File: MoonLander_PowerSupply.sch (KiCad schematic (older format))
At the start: 17 parts

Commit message: first whack at layout - unrouted
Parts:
- removed C?: 1uF, symbol C
- C201: renamed from C?; value 1Uf -> 1uF; footprint (none) -> Capacitors_SMD:C_0402
- C202, C204: renamed from C?; footprint (none) -> Capacitors_SMD:C_0402
- D201: renamed from D?; footprint (none) -> Diodes_SMD:SOD-323
- D202, D203: renamed from D?; footprint (none) -> LEDs:LED-0603
- IC201: renamed from IC?; footprint (none) -> GrayCatLabs:TI-DSQ
- IC202: renamed from IC?; footprint (none) -> GrayCatLabs:SSOP5
- R201, R202, R203, R204, R205, R206, R207, R208: renamed from R?; footprint (none) -> Resistors_SMD:R_0402
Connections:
- net GND: now also IC201.3 (VSS)
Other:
- moved on the sheet: C202
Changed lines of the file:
@@
 $EndDescr
 $Comp
-L LED D?
+L LED D202
 U 1 1 565F7410
 P 5600 3200
-F 0 "D?" H 5600 3300 50  0000 C CNN
+F 0 "D202" H 5600 3300 50  0000 C CNN
 F 1 "LED" H 5600 3100 50  0000 C CNN
-F 2 "" H 5600 3200 50  0000 C CNN
+F 2 "LEDs:LED-0603" H 5600 3200 50  0001 C CNN
 F 3 "" H 5600 3200 50  0000 C CNN
 	1    5600 3200
@@
 $EndComp
 $Comp
-L R R?
+L R R205
 U 1 1 565F74DB
 P 5350 3600
-F 0 "R?" V 5430 3600 50  0000 C CNN
+F 0 "R205" V 5430 3600 50  0000 C CNN
 F 1 "1k" V 5350 3600 50  0000 C CNN
-F 2 "" V 5280 3600 50  0000 C CNN
+F 2 "Resistors_SMD:R_0402" V 5280 3600 50  0001 C CNN
 F 3 "" H 5350 3600 50  0000 C CNN
 	1    5350 3600
@@
 $EndComp
 $Comp
-L C C?
+L C C201
 U 1 1 565F75E8
 P 2300 3600
-F 0 "C?" H 2325 3700 50  0000 L CNN
-F 1 "1Uf" H 2325 3500 50  0000 L CNN
-F 2 "" H 2338 3450 50  0000 C CNN
+F 0 "C201" H 2325 3700 50  0000 L CNN
+F 1 "1uF" H 2325 3500 50  0000 L CNN
+F 2 "Capacitors_SMD:C_0402" H 2338 3450 50  0001 C CNN
 F 3 "" H 2300 3600 50  0000 C CNN
 	1    2300 3600
@@
 $EndComp
 Wire Wire Line
-	2300 3000 2300 3300
-Wire Wire Line
-	2300 3300 2300 3450
-$Comp
-L GND #PWR?
+	2300 3000 2300 3450
+$Comp
+L GND #PWR05
 U 1 1 565F7639
 P 2300 4050
-F 0 "#PWR?" H 2300 3800 50  0001 C CNN
+F 0 "#PWR05" H 2300 3800 50  0001 C CNN
 F 1 "GND" H 2300 3900 50  0000 C CNN
 F 2 "" H 2300 4050 50  0000 C CNN
@@
 $EndComp
 Wire Wire Line
-	2300 3750 2300 4000
-Wire Wire Line
-	2300 4000 2300 4050
+	2300 3750 2300 4050
 Connection ~ 2300 3300
 $Comp
-L 5V_USB #PWR?
+L 5V_USB #PWR06
 U 1 1 565F7A7B
 P 2300 3000
-F 0 "#PWR?" H 2300 2850 50  0001 C CNN
+F 0 "#PWR06" H 2300 2850 50  0001 C CNN
 F 1 "5V_USB" H 2300 3140 50  0000 C CNN
 F 2 "" H 2300 3000 60  0000 C CNN
@@
 V_BAT
 $Comp
-L BQ24040/5 IC?
+L BQ24040/5 IC201
 U 1 1 56602B0A
 P 4100 3550
-F 0 "IC?" H 3900 3950 60  0000 C CNN
+F 0 "IC201" H 3900 3950 60  0000 C CNN
 F 1 "BQ24040/5" H 4150 3100 60  0000 C CNN
-F 2 "" H 4100 3550 60  0000 C CNN
+F 2 "GrayCatLabs:TI-DSQ" H 4100 3550 60  0001 C CNN
 F 3 "" H 4100 3550 60  0000 C CNN
 	1    4100 3550
@@
 $EndComp
 Wire Wire Line
-	2300 3300 2800 3300
-Wire Wire Line
-	2800 3300 3600 3300
+	2300 3300 3600 3300
 Wire Wire Line
 	5300 3300 4600 3300
 $Comp
-L R R?
+L R R204
 U 1 1 56602B85
 P 4900 3450
-F 0 "R?" V 4980 3450 50  0000 C CNN
+F 0 "R204" V 4980 3450 50  0000 C CNN
 F 1 "10k" V 4900 3450 50  0000 C CNN
-F 2 "" V 4830 3450 50  0000 C CNN
+F 2 "Resistors_SMD:R_0402" V 4830 3450 50  0001 C CNN
 F 3 "" H 4900 3450 50  0000 C CNN
 	1    4900 3450
@@
 	3600 3750 3450 3750
 Wire Wire Line
-	3450 3750 3450 4000
-Wire Wire Line
-	3450 4000 3150 4000
-Wire Wire Line
-	3150 4000 2800 4000
-Wire Wire Line
-	2800 4000 2300 4000
+	3450 4000 3450 3650
+Wire Wire Line
+	2300 4000 3450 4000
 Connection ~ 2300 4000
 $Comp
-L R R?
+L R R202
 U 1 1 56602F23
 P 3150 3750
-F 0 "R?" V 3230 3750 50  0000 C CNN
+F 0 "R202" V 3230 3750 50  0000 C CNN
 F 1 "2k" V 3150 3750 50  0000 C CNN
-F 2 "" V 3080 3750 50  0000 C CNN
+F 2 "Resistors_SMD:R_0402" V 3080 3750 50  0001 C CNN
 F 3 "" H 3150 3750 50  0000 C CNN
 	1    3150 3750
@@
 $EndComp
 $Comp
-L R R?
+L R R201
 U 1 1 56602F6D
 P 2800 3750
-F 0 "R?" V 2880 3750 50  0000 C CNN
+F 0 "R201" V 2880 3750 50  0000 C CNN
 F 1 "1k" V 2800 3750 50  0000 C CNN
-F 2 "" V 2730 3750 50  0000 C CNN
+F 2 "Resistors_SMD:R_0402" V 2730 3750 50  0001 C CNN
 F 3 "" H 2800 3750 50  0000 C CNN
 	1    2800 3750
@@
 	2800 3450 2800 3600
 $Comp
-L C C?
+L C C202
 U 1 1 566031DD
-P 6500 3250
-F 0 "C?" H 6525 3350 50  0000 L CNN
-F 1 "1uF" H 6525 3150 50  0000 L CNN
-F 2 "" H 6538 3100 50  0000 C CNN
-F 3 "" H 6500 3250 50  0000 C CNN
-	1    6500 3250
-	1    0    0    -1
-$EndComp
-$Comp
-L GND #PWR?
+P 6650 3250
+F 0 "C202" H 6675 3350 50  0000 L CNN
+F 1 "1uF" H 6675 3150 50  0000 L CNN
+F 2 "Capacitors_SMD:C_0402" H 6688 3100 50  0001 C CNN
+F 3 "" H 6650 3250 50  0000 C CNN
+	1    6650 3250
+	1    0    0    -1
+$EndComp
+$Comp
+L GND #PWR07
 U 1 1 56603249
-P 6500 3650
-F 0 "#PWR?" H 6500 3400 50  0001 C CNN
-F 1 "GND" H 6500 3500 50  0000 C CNN
-F 2 "" H 6500 3650 50  0000 C CNN
-F 3 "" H 6500 3650 50  0000 C CNN
-	1    6500 3650
-	1    0    0    -1
-$EndComp
-Wire Wire Line
-	6500 3400 6500 3550
-Wire Wire Line
-	6500 3550 6500 3650
-Wire Wire Line
-	6500 2900 6500 3100
+P 6650 3650
+F 0 "#PWR07" H 6650 3400 50  0001 C CNN
+F 1 "GND" H 6650 3500 50  0000 C CNN
+F 2 "" H 6650 3650 50  0000 C CNN
+F 3 "" H 6650 3650 50  0000 C CNN
+	1    6650 3650
+	1    0    0    -1
+$EndComp
+Wire Wire Line
+	6650 3400 6650 3650
+Wire Wire Line
+	6650 2900 6650 3100
 Connection ~ 5600 2900
 $Comp
-L LED D?
+L LED D203
 U 1 1 566037A1
 P 6000 3200
-F 0 "D?" H 6000 3300 50  0000 C CNN
+F 0 "D203" H 6000 3300 50  0000 C CNN
 F 1 "LED" H 6000 3100 50  0000 C CNN
-F 2 "" H 6000 3200 50  0000 C CNN
+F 2 "LEDs:LED-0603" H 6000 3200 50  0001 C CNN
 F 3 "" H 6000 3200 50  0000 C CNN
 	1    6000 3200
@@
 $EndComp
 $Comp
-L R R?
+L R R207
 U 1 1 566037A7
 P 5750 3700
-F 0 "R?" V 5830 3700 50  0000 C CNN
+F 0 "R207" V 5830 3700 50  0000 C CNN
 F 1 "1k" V 5750 3700 50  0000 C CNN
-F 2 "" V 5680 3700 50  0000 C CNN
+F 2 "Resistors_SMD:R_0402" V 5680 3700 50  0001 C CNN
 F 3 "" H 5750 3700 50  0000 C CNN
 	1    5750 3700
@@
 	4850 4000 4850 3850
 Wire Wire Line
-	4600 3850 4850 3850
-Wire Wire Line
-	4850 3850 5300 3850
-$Comp
-L R R?
+	4600 3850 5300 3850
+$Comp
+L R R203
 U 1 1 56603E4F
 P 4850 4150
-F 0 "R?" V 4930 4150 50  0000 C CNN
+F 0 "R203" V 4930 4150 50  0000 C CNN
 F 1 "100k" V 4850 4150 50  0000 C CNN
-F 2 "" V 4780 4150 50  0000 C CNN
+F 2 "Resistors_SMD:R_0402" V 4780 4150 50  0001 C CNN
 F 3 "" H 4850 4150 50  0000 C CNN
 	1    4850 4150
@@
 $EndComp
 $Comp
-L GND #PWR?
+L GND #PWR08
 U 1 1 56603E8A
 P 4850 4450
-F 0 "#PWR?" H 4850 4200 50  0001 C CNN
+F 0 "#PWR08" H 4850 4200 50  0001 C CNN
 F 1 "GND" H 4850 4300 50  0000 C CNN
 F 2 "" H 4850 4450 50  0000 C CNN
@@
 Connection ~ 4850 3850
 $Comp
-L R R?
+L R R206
 U 1 1 56604088
 P 5700 4650
-F 0 "R?" V 5780 4650 50  0000 C CNN
+F 0 "R206" V 5780 4650 50  0000 C CNN
 F 1 "0" V 5700 4650 50  0000 C CNN
-F 2 "" V 5630 4650 50  0000 C CNN
+F 2 "Resistors_SMD:R_0402" V 5630 4650 50  0001 C CNN
 F 3 "" H 5700 4650 50  0000 C CNN
 	1    5700 4650
@@
 	5700 4900 5700 4800
 $Comp
-L VCC #PWR?
+L VCC #PWR09
 U 1 1 566041E5
 P 5700 4400
-F 0 "#PWR?" H 5700 4250 50  0001 C CNN
+F 0 "#PWR09" H 5700 4250 50  0001 C CNN
 F 1 "VCC" H 5700 4550 50  0000 C CNN
 F 2 "" H 5700 4400 50  0000 C CNN
@@
 Text Notes 5850 4850 0    60   ~ 0
 Populate for 500mA fast charge\n\nCharge current set by ISET resistor\nif not populated
-Connection ~ 6500 2900
+Connection ~ 6650 2900
 Wire Wire Line
 	5300 2900 5300 3300
 $Comp
-L GND #PWR?
+L GND #PWR010
 U 1 1 56606519
 P 5100 3450
-F 0 "#PWR?" H 5100 3200 50  0001 C CNN
+F 0 "#PWR010" H 5100 3200 50  0001 C CNN
 F 1 "GND" H 5100 3300 50  0000 C CNN
 F 2 "" H 5100 3450 50  0000 C CNN
@@
 V_EXT
 $Comp
-L D_Schottky D?
+L D_Schottky D201
 U 1 1 5660777F
 P 2800 2800
-F 0 "D?" H 2800 2900 50  0000 C CNN
+F 0 "D201" H 2800 2900 50  0000 C CNN
 F 1 "D_Schottky" H 2800 2700 50  0000 C CNN
-F 2 "" H 2800 2800 50  0000 C CNN
+F 2 "Diodes_SMD:SOD-323" H 2800 2800 50  0001 C CNN
 F 3 "" H 2800 2800 50  0000 C CNN
 	1    2800 2800
@@
 Connection ~ 2800 3300
 Wire Wire Line
-	5150 2900 5300 2900
-Wire Wire Line
-	5300 2900 5600 2900
-Wire Wire Line
-	5600 2900 6000 2900
-Wire Wire Line
-	6000 2900 6500 2900
-Wire Wire Line
-	6500 2900 6900 2900
-Wire Wire Line
-	6900 2900 7350 2900
-Wire Wire Line
-	7350 2900 7900 2900
-$Comp
-L BUxxSD5 IC?
+	5150 2900 7900 2900
+$Comp
+L BUxxSD5 IC202
 U 1 1 565FCD4F
 P 8350 3050
-F 0 "IC?" H 8200 3350 60  0000 C CNN
+F 0 "IC202" H 8200 3350 60  0000 C CNN
 F 1 "BU33SD5" H 8400 2750 60  0000 C CNN
-F 2 "" H 8350 3050 60  0000 C CNN
+F 2 "GrayCatLabs:SSOP5" H 8350 3050 60  0001 C CNN
 F 3 "" H 8350 3050 60  0000 C CNN
 	1    8350 3050
@@
 $EndComp
 $Comp
-L R R?
+L R R208
 U 1 1 565FD0F5
 P 7650 3050
-F 0 "R?" V 7730 3050 50  0000 C CNN
+F 0 "R208" V 7730 3050 50  0000 C CNN
 F 1 "100k" V 7650 3050 50  0000 C CNN
-F 2 "" V 7580 3050 50  0000 C CNN
+F 2 "Resistors_SMD:R_0402" V 7580 3050 50  0001 C CNN
 F 3 "" H 7650 3050 50  0000 C CNN
 	1    7650 3050
@@
 	7750 3200 7750 3550
 Wire Wire Line
-	6500 3550 6900 3550
-Wire Wire Line
-	6900 3550 7750 3550
-Wire Wire Line
-	7750 3550 9600 3550
-Connection ~ 6500 3550
+	6650 3550 9600 3550
+Connection ~ 6650 3550
 Wire Wire Line
 	8800 2900 9600 2900
 Wire Wire Line
-	9600 2750 9600 2900
-Wire Wire Line
-	9600 2900 9600 3100
-$Comp
-L C C?
+	9600 2750 9600 3100
+$Comp
+L C C204
 U 1 1 565FD299
 P 9600 3250
-F 0 "C?" H 9625 3350 50  0000 L CNN
+F 0 "C204" H 9625 3350 50  0000 L CNN
 F 1 "1uF" H 9625 3150 50  0000 L CNN
-F 2 "" H 9638 3100 50  0000 C CNN
+F 2 "Capacitors_SMD:C_0402" H 9638 3100 50  0001 C CNN
 F 3 "" H 9600 3250 50  0000 C CNN
 	1    9600 3250
@@
 Connection ~ 9600 2900
 $Comp
-L VCC #PWR?
+L VCC #PWR011
 U 1 1 565FD3E2
 P 9600 2750
-F 0 "#PWR?" H 9600 2600 50  0001 C CNN
+F 0 "#PWR011" H 9600 2600 50  0001 C CNN
 F 1 "VCC" H 9600 2900 50  0000 C CNN
 F 2 "" H 9600 2750 50  0000 C CNN
@@
 	1    0    0    -1
 $EndComp
-$Comp
-L C C?
-U 1 1 565FE03A
-P 6900 3250
-F 0 "C?" H 6925 3350 50  0000 L CNN
-F 1 "1uF" H 6925 3150 50  0000 L CNN
-F 2 "" H 6938 3100 50  0000 C CNN
-F 3 "" H 6900 3250 50  0000 C CNN
-	1    6900 3250
-	1    0    0    -1
-$EndComp
-Wire Wire Line
-	6900 3100 6900 2900
-Connection ~ 6900 2900
-Wire Wire Line
-	6900 3400 6900 3550
-Connection ~ 6900 3550
+Wire Wire Line
+	3450 3650 3600 3650
+Connection ~ 3450 3750
 $EndSCHEMATC

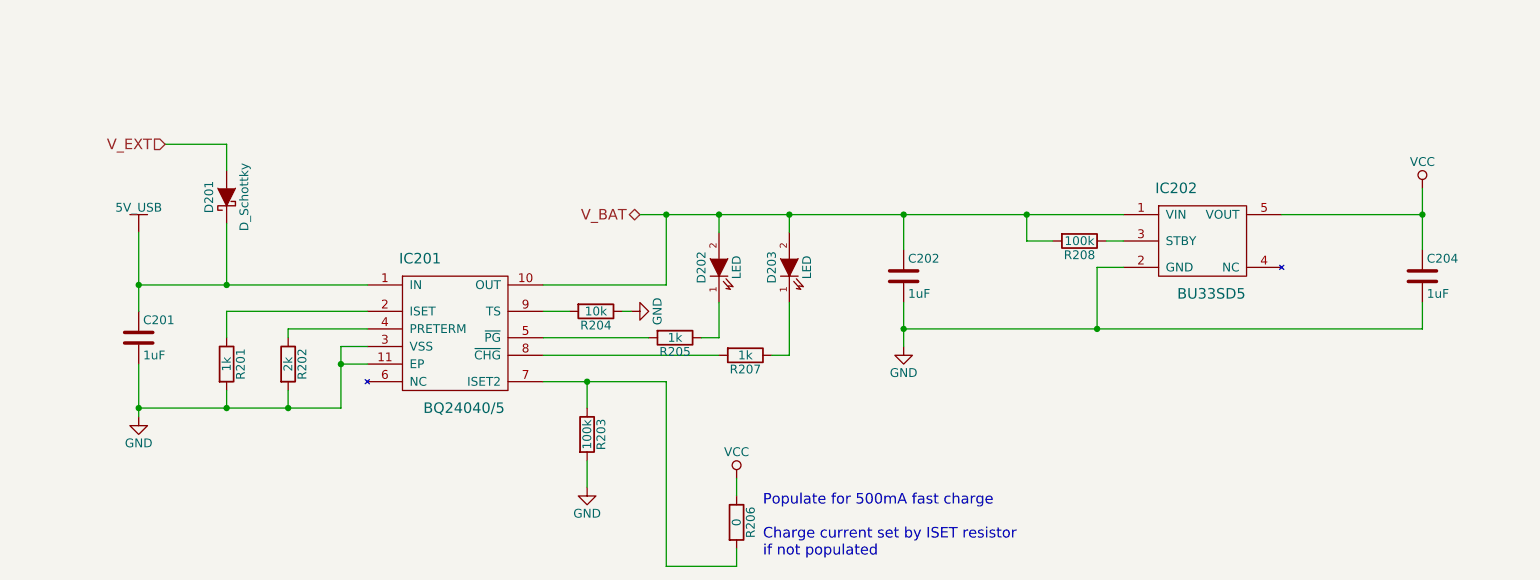
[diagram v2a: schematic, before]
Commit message: simplified 2 layer version
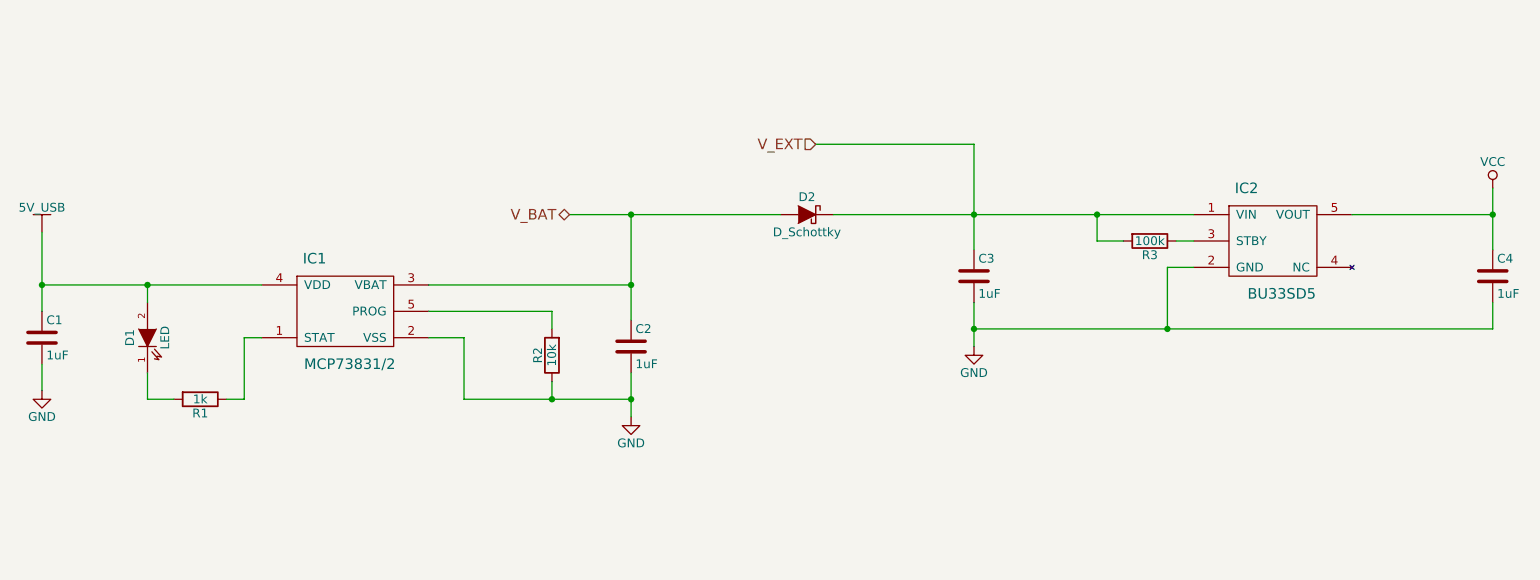
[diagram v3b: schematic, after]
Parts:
- removed D203: LED, LEDs:LED-0603, symbol LED
- removed IC201: BQ24040/5, GrayCatLabs:TI-DSQ, symbol BQ24040/5
- removed R201, R207: 1k, Resistors_SMD:R_0402, symbol R
- removed R202: 2k, Resistors_SMD:R_0402, symbol R
- removed R203: 100k, Resistors_SMD:R_0402, symbol R
- removed R206: 0, Resistors_SMD:R_0402, symbol R
- added C2: 1uF, Capacitors_SMD:C_0402, symbol C
- added IC1: MCP73831/2, GrayCatLabs:SSOP5, symbol MCP73831/2
- renumbered C201 to C1, C202 to C3, C204 to C4, D202 to D1, D201 to D2, IC202 to IC2, R205 to R1, R204 to R2, R208 to R3
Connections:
- net 5V_USB: now also D1.2 (A), IC1.4 (VDD); no longer D2.1 (K)
- net GND: now also C2.2, IC1.2 (VSS)
- net V_BAT: now also D2.2 (A), C2.1, IC1.3 (VBAT); no longer C3.1, D1.2 (A), IC2.1 (VIN), R3.2
- net V_EXT: now also C3.1, D2.1 (K), IC2.1 (VIN), R3.2; no longer D2.2 (A)
- net at D1.1 (K): now also R1.2; no longer R1.1
- net at R2.2: now also IC1.5 (PROG)
- new net: IC1.1 (STAT), R1.1
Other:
- note removed: "Populate for 500mA fast charge\n\nCharge current set by ISET resistor\nif not populated"
- moved on the sheet: C1, C3, C4, D1, D2, IC2, R1, R2, R3
